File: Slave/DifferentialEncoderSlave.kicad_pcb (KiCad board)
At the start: 4 copper layers, 52.5 x 35.2 mm, 15 parts, among them J1 Conn_01x04, U1 LTC2850xS8, U2 MA730, U3 AZ1117-3.3

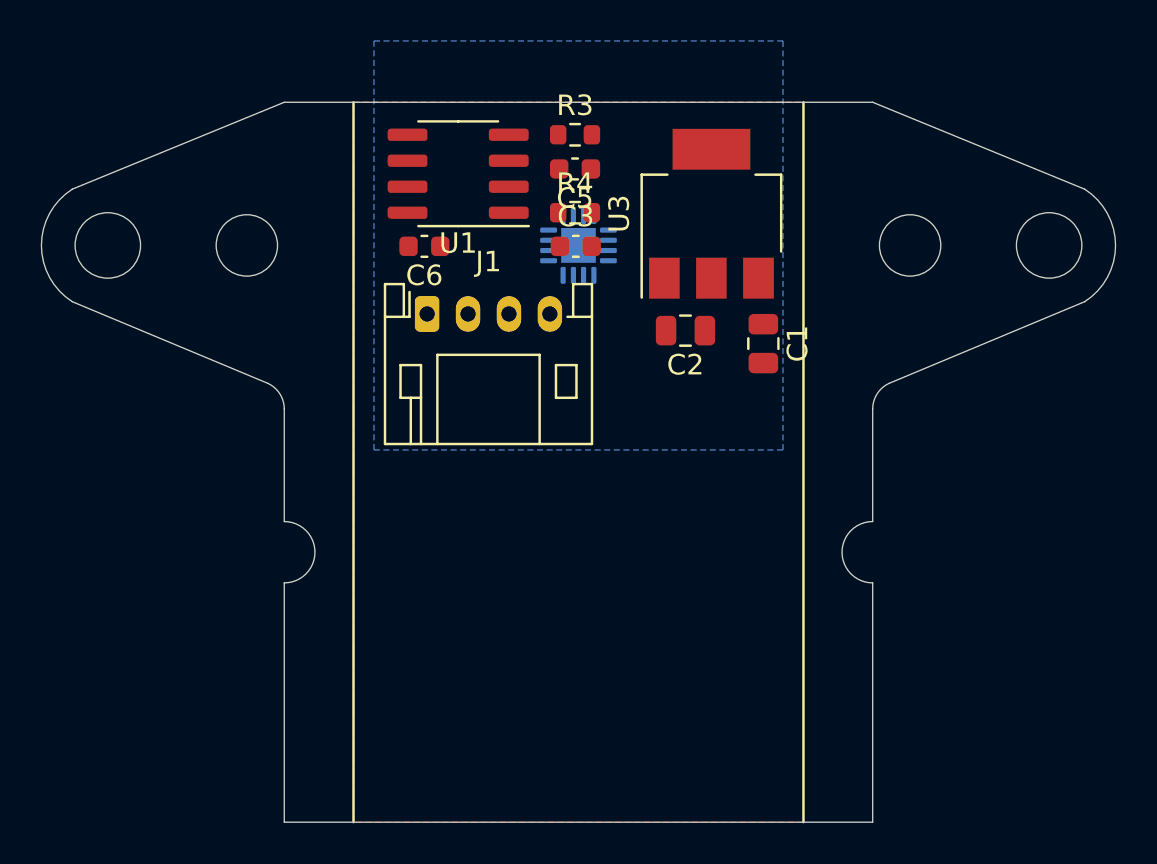
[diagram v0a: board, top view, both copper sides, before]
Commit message: Finish laying out encoder board
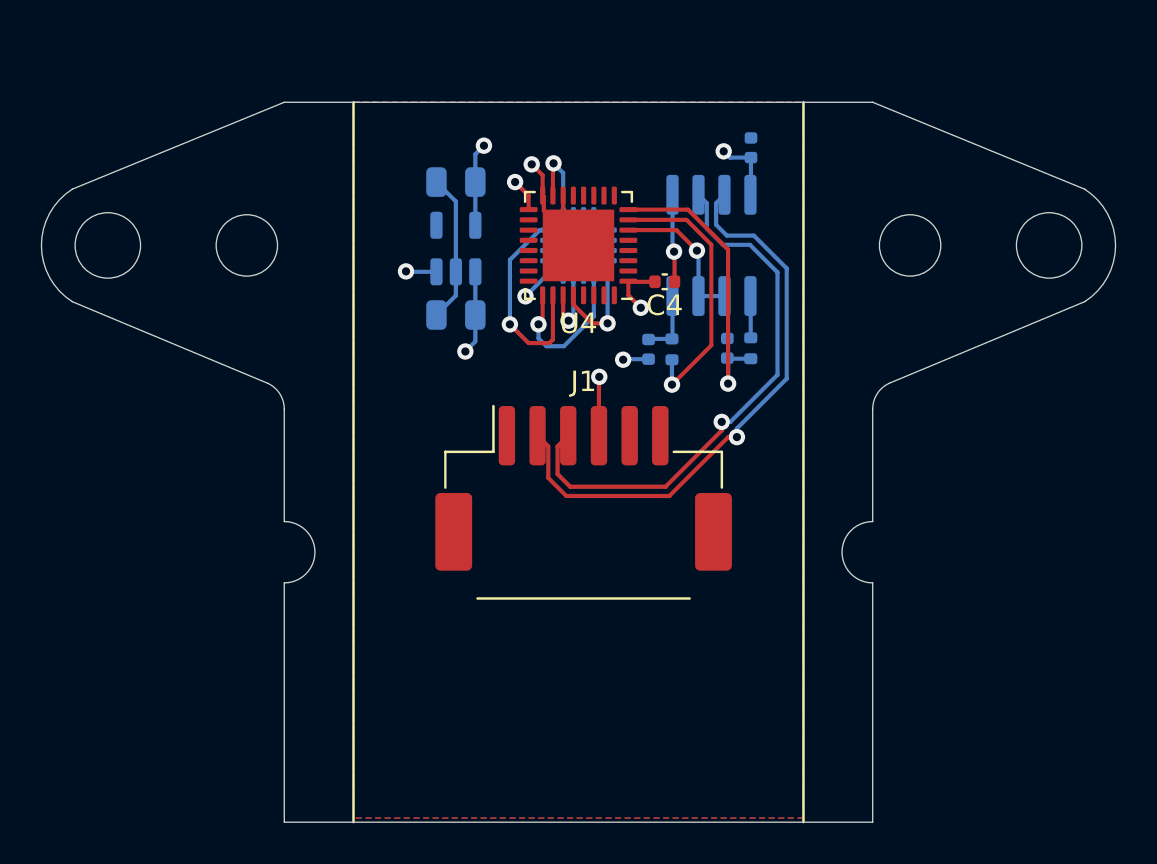
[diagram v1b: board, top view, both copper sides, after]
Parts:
- removed the U3 at (128.5, 66.5)
- added C4: 100nF, Capacitor_SMD:C_0402_1005Metric, F.Cu at (126.2, 69.8)
- added U2: LP5907MFX-3.3, Package_TO_SOT_SMD:SOT-23-5, B.Cu at (116.0, 68.2)
- added U4: STM32G4A1KEU4, Package_DFN_QFN:UFQFPN-32-1EP_5x5mm_P0.5mm_EP3.5x3.5mm, F.Cu at (122.0, 68.0)
- C1: renamed from C6; footprint Capacitor_SMD:C_0603_1608Metric -> Capacitor_SMD:C_0402_1005Metric; moved to B.Cu
- C2: renamed from C3; footprint Capacitor_SMD:C_0603_1608Metric -> Capacitor_SMD:C_0402_1005Metric; moved to B.Cu
- C3: renamed from C5; footprint Capacitor_SMD:C_0603_1608Metric -> Capacitor_SMD:C_0402_1005Metric; moved to B.Cu
- C5: renamed from C1; moved to B.Cu
- C6: renamed from C2; moved to B.Cu
- J1: value Conn_01x04 -> Conn_01x06; footprint Connector_JST:JST_PH_S4B-PH-K_1x04_P2.00mm_Horizontal -> Connector_Molex:Molex_CLIK-Mate_502585-0670_1x06-1MP_P1.50mm_Horizontal
- R1: renamed from R4; footprint Resistor_SMD:R_0603_1608Metric -> Resistor_SMD:R_0402_1005Metric; moved to B.Cu
- R2: renamed from R3; footprint Resistor_SMD:R_0603_1608Metric -> Resistor_SMD:R_0402_1005Metric; moved to B.Cu
- U1: moved to B.Cu
- moved C1 16.7 mm to (130.4, 63.2), turned to -90 degrees
- moved C5 15.1 mm to (116.0, 71.4), turned to 180 degrees
- moved C6 13.4 mm to (116.0, 64.9)
- moved U1 12.9 mm to (128.5, 68.0), turned to 90 degrees
- moved R2 11.5 mm to (126.6, 73.1), turned to -90 degrees
- moved J1 11.5 mm to (122.2, 79.9)
- moved R1 10.9 mm to (130.4, 73.0), turned to -90 degrees
- moved C3 9.52 mm to (125.4, 73.1), turned to 90 degrees
- moved C2 8.93 mm to (129.3, 73.0), turned to -90 degrees
- renumbered U2 to U3
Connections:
- net /RS485_B renamed /RS485_-
- net /UART_RX renamed /USART2_RX
- J1 pad 1: /RS485_A -> +5V
- J1 pad 3: +5V -> /RS485_+
- R2 pad 2: /UART_TX -> /USART2_TX
- U1 pad 2: /~{RE} -> /USART2_DE
- U1 pad 3: /DE -> /USART2_DE
- U1 pad 6: /RS485_A -> /RS485_+
- U3 pad 12: /CLK -> /SPI3_SCK
- U3 pad 4: unconnected-(U2-Pad4) -> /SPI3_MOSI
- U3 pad 5: /CSn -> /SPI3_NSS
- U3 pad 7: /MISO -> /SPI3_MISO
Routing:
- net GNDD: track 0.00 -> 29.0 mm, vias 0 -> 5
- net /RS485_-: track 0.00 -> 28.3 mm, vias 0 -> 1
- net /RS485_+: track 0.00 -> 26.8 mm, vias 0 -> 1
- net /USART2_RX: track 0.00 -> 14.7 mm, vias 0 -> 1
- net /USART2_TX: track 0.00 -> 13.4 mm, vias 0 -> 1
- net +3V3: track 0.00 -> 12.9 mm, vias 0 -> 4
- net /SPI3_SCK: track 0.00 -> 10.4 mm, vias 0 -> 1
- net +5V: track 0.00 -> 8.88 mm, vias 0 -> 3
- net /SPI3_NSS: track 0.00 -> 7.67 mm, vias 0 -> 1
- net /USART2_DE: track 0.00 -> 7.29 mm, vias 0 -> 1
- net /SPI3_MOSI: track 0.00 -> 5.58 mm, vias 0 -> 1
- net /SPI3_MISO: track 0.00 -> 3.67 mm, vias 0 -> 1
- net /DI: track 0.00 -> 3.30 mm
- net /RO: track 0.00 -> 2.05 mm
- added copper zone on In1.Cu, net +3V3
- added copper zone on F.Cu, net +5V
- removed copper zone on F.Cu, net +3V3
- removed copper zone on In1.Cu, net +5V

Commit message: Change pinout on STM32G4, add thermistor header, add test points
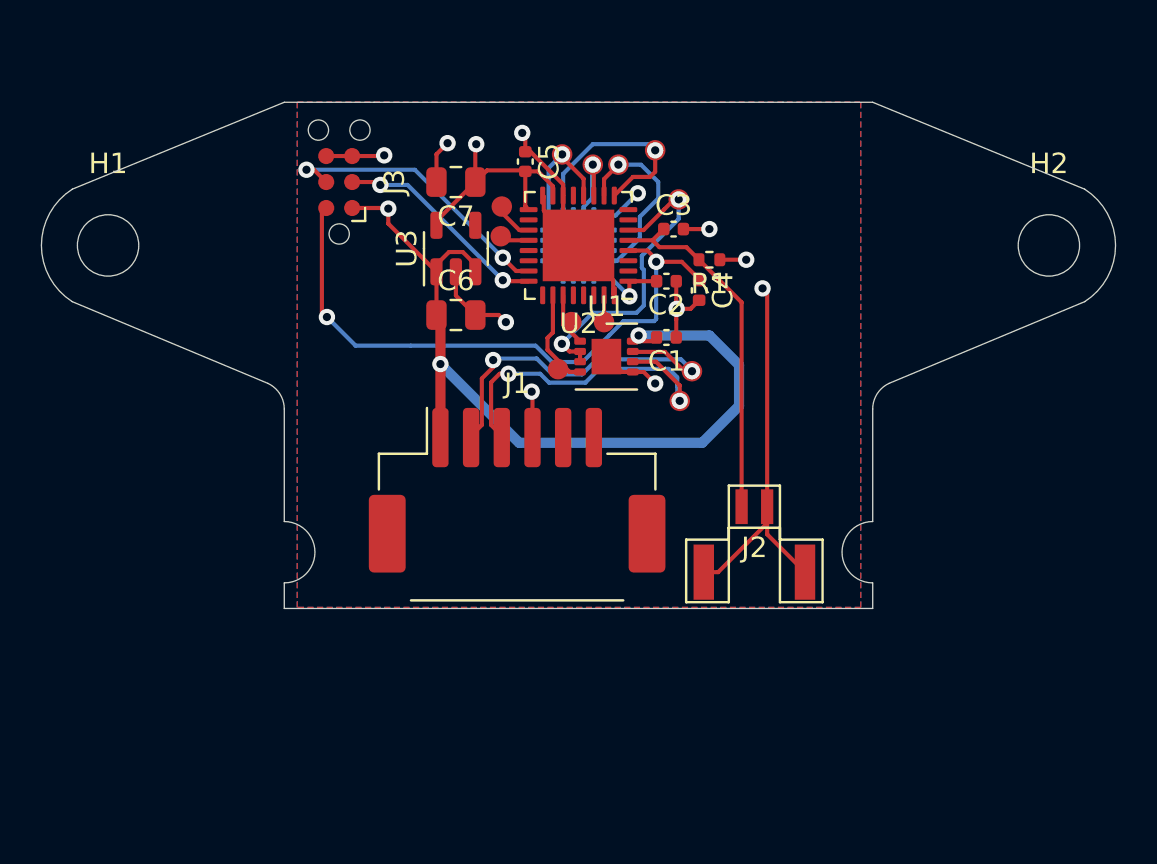
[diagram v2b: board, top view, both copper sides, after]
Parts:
- removed the C2 at (129.3, 73.0)
- removed H3: MountingHole, MountingHole:MountingHole_3mm
- removed H5, H6: MountingHole, MountingHole:MountingHole_3.2mm_M3_DIN965
- removed R2: 680, Resistor_SMD:R_0402_1005Metric
- added C4: 100nF, Capacitor_SMD:C_0402_1005Metric, F.Cu at (127.9, 70.2)
- added C5: 100nF, Capacitor_SMD:C_0402_1005Metric, F.Cu at (119.4, 63.9)
- added H2: MountingHole, MountingHole:MountingHole_3mm, F.Cu at (145.0, 68.0)
- added J2: Thermistor, ODrive_KiCad:JST_GH_SM02B, F.Cu at (130.6, 80.8)
- added J3: Conn_01x06, Connector:Tag-Connect_TC2030-IDC-NL_2x03_P1.27mm_Vertical, F.Cu at (110.3, 64.9)
- added TP1: TestPoint, ODrive_KiCad:TestPoint_Pad_D1.0mm, F.Cu at (123.2, 71.8)
- added TP10: TestPoint, ODrive_KiCad:TestPoint_Pad_D1.0mm, F.Cu at (121.2, 63.5)
- added TP11: TestPoint, ODrive_KiCad:TestPoint_Pad_D1.0mm, F.Cu at (127.5, 74.2)
- added TP12: TestPoint, ODrive_KiCad:TestPoint_Pad_D1.0mm, F.Cu at (127.0, 75.6)
- added TP2: TestPoint, ODrive_KiCad:TestPoint_Pad_D1.0mm, F.Cu at (118.2, 66.1)
- added TP3: TestPoint, ODrive_KiCad:TestPoint_Pad_D1.0mm, F.Cu at (118.2, 67.5)
- added TP4: TestPoint, ODrive_KiCad:TestPoint_Pad_D1.0mm, F.Cu at (126.9, 65.8)
- added TP5: TestPoint, ODrive_KiCad:TestPoint_Pad_D1.0mm, F.Cu at (121.0, 74.0)
- added TP6: TestPoint, ODrive_KiCad:TestPoint_Pad_D1.0mm, F.Cu at (121.7, 71.8)
- added TP7: TestPoint, ODrive_KiCad:TestPoint_Pad_D1.0mm, F.Cu at (125.8, 63.4)
- added TP8: TestPoint, ODrive_KiCad:TestPoint_Pad_D1.0mm, F.Cu at (124.0, 64.0)
- added TP9: TestPoint, ODrive_KiCad:TestPoint_Pad_D1.0mm, F.Cu at (122.7, 64.0)
- C1: moved to F.Cu
- C3: value 22pF -> 2.2uF; moved to F.Cu
- C6: renamed from C5; moved to F.Cu
- C7: renamed from C6; moved to F.Cu
- J1: value Conn_01x06 -> Main
- R1: value 680 -> 4.7k; moved to F.Cu
- U1: value LTC2850xS8 -> ADM4852; footprint Package_SO:SOIC-8_3.9x4.9mm_P1.27mm -> Package_CSP:LFCSP-8-1EP_3x3mm_P0.5mm_EP1.45x1.74mm; moved to F.Cu
- U3: renamed from U2; moved to F.Cu
- moved H1 39.2 mm to (99.0, 68.0)
- moved C1 10.2 mm to (126.3, 72.5), turned to 180 degrees
- moved U1 7.48 mm to (123.4, 73.4), turned to 0 degrees
- moved C3 6.01 mm to (126.7, 67.2), turned to 0 degrees
- moved R1 4.78 mm to (128.4, 68.7), turned to 180 degrees
- moved J1 3.25 mm to (119.0, 80.0)
- moved C2 0.09 mm to (126.3, 69.8)
- turned C6 to 0 degrees
- turned U4 to 0 degrees
- renumbered C4 to C2, U4 to U2, U3 to U4
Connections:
- net /RS485_+ renamed /RS485_P
- net /RS485_- renamed /RS485_N
- net /USB_DM renamed /USB_DN
- C3 pad 1: GNDD -> /TEMP
- C3 pad 2: /DI -> GNDD
- R1 pad 1: /RO -> +3V3
- R1 pad 2: /USART2_RX -> /TEMP
- U1 pad 1: /RO -> /USART2_RX
- U1 pad 4: /DI -> /USART2_TX
- U2 pad 10: unconnected-(U4-Pad10) -> /SPI1_SCK
- U2 pad 11: unconnected-(U4-Pad11) (its old number) -> /SPI1_MISO
- U2 pad 12: /ADC2_IN4 -> /SPI1_MOSI
- U2 pad 13: /ADC1_IN15 -> unconnected-(U2-Pad13)
- U2 pad 19: unconnected-(U4-Pad19) -> /USART1_TX
- U2 pad 20: unconnected-(U4-Pad20) -> /USART1_RX
- U2 pad 23: unconnected-(U4-Pad23) -> /SWDIO
- U2 pad 24: unconnected-(U4-Pad24) -> /SWCLK
- U2 pad 25: /SPI3_NSS -> unconnected-(U2-Pad25)
- U2 pad 26: /SPI3_SCK -> /USART2_TX
- U2 pad 27: /SPI3_MISO -> /USART2_RX
- U2 pad 28: /SPI3_MOSI -> /I2S3_SD
- U2 pad 31: (no net) -> /BOOT0
- U2 pad 32: (no net) -> GNDD
- U2 pad 4: (no net) -> /~{RESET}
- U2 pad 5: /ADC1_IN1 -> /TEMP
- U2 pad 7: /USART2_TX -> unconnected-(U2-Pad7)
- U2 pad 8: /USART2_RX -> unconnected-(U2-Pad8)
- U2 pad 9: unconnected-(U4-Pad9) (its old number) -> /SPI1_NSS
- U4 pad 12: /SPI3_SCK -> /SPI1_SCK
- U4 pad 4: /SPI3_MOSI -> /SPI1_MOSI
- U4 pad 5: /SPI3_NSS -> /SPI1_NSS
- U4 pad 7: /SPI3_MISO -> /SPI1_MISO
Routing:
- net +5V: track 8.88 -> 43.2 mm
- net GNDD: track 29.0 -> 59.9 mm, vias 5 -> 10
- net /~{RESET}: track 0.00 -> 30.3 mm, vias 0 -> 2
- net /TEMP: track 0.00 -> 17.6 mm
- net /SWDIO: track 0.00 -> 14.1 mm, vias 0 -> 2
- net /USART2_RX: track 14.7 -> 2.59 mm, vias 1 -> 0
- net /SPI1_NSS: track 0.00 -> 10.8 mm, vias 0 -> 1
- net /SWCLK: track 0.00 -> 10.6 mm, vias 0 -> 2
- net /SPI3_SCK: track 10.4 -> 0.00 mm, vias 1 -> 0
- net /RS485_N: track 28.3 -> 18.1 mm, vias 1 -> 2
- net /RS485_P: track 26.8 -> 17.5 mm, vias 1 -> 2
- net /SPI1_SCK: track 0.00 -> 9.21 mm, vias 0 -> 1
- net /USART2_TX: track 13.4 -> 4.82 mm, vias 1 -> 0
- net /USART2_DE: track 7.29 -> 15.4 mm, vias 1 -> 2
- net /SPI3_NSS: track 7.67 -> 0.00 mm, vias 1 -> 0
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- added copper zone on B.Cu, net +5V
- added copper zone on F.Cu, net GNDD
- removed copper zone on F.Cu, net +5V
- removed copper zone on B.Cu, net GNDD
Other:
- board size 52.5 x 35.2 mm -> 52.5 x 24.8 mm

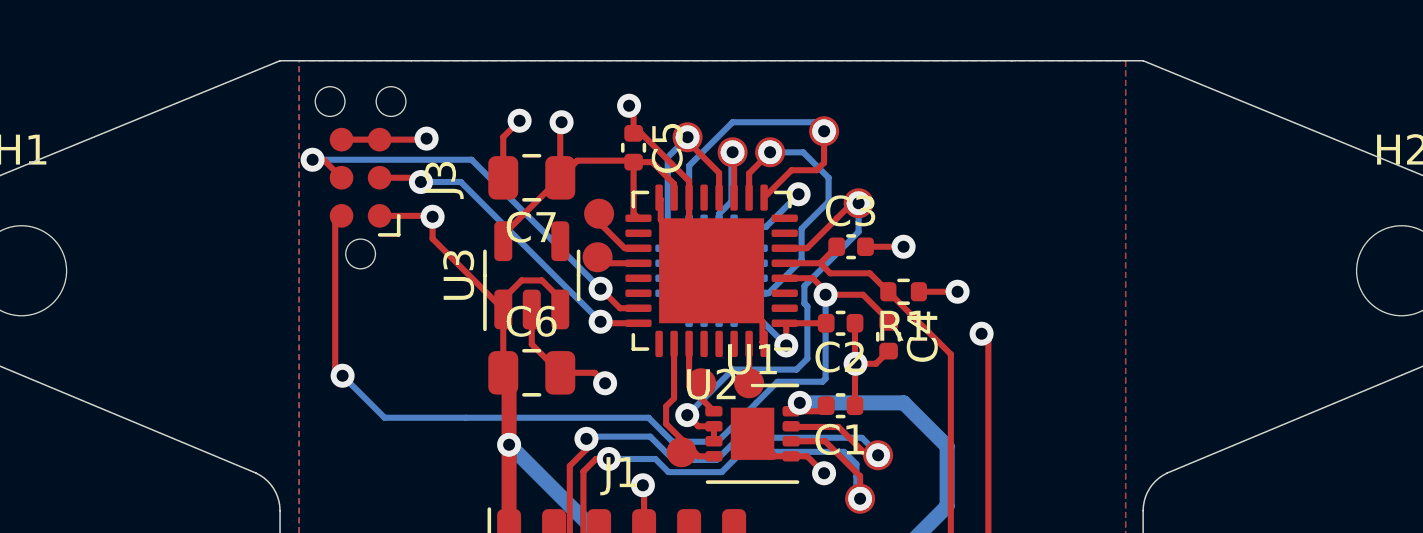
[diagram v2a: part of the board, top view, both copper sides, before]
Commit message: Add narrow mounting holes
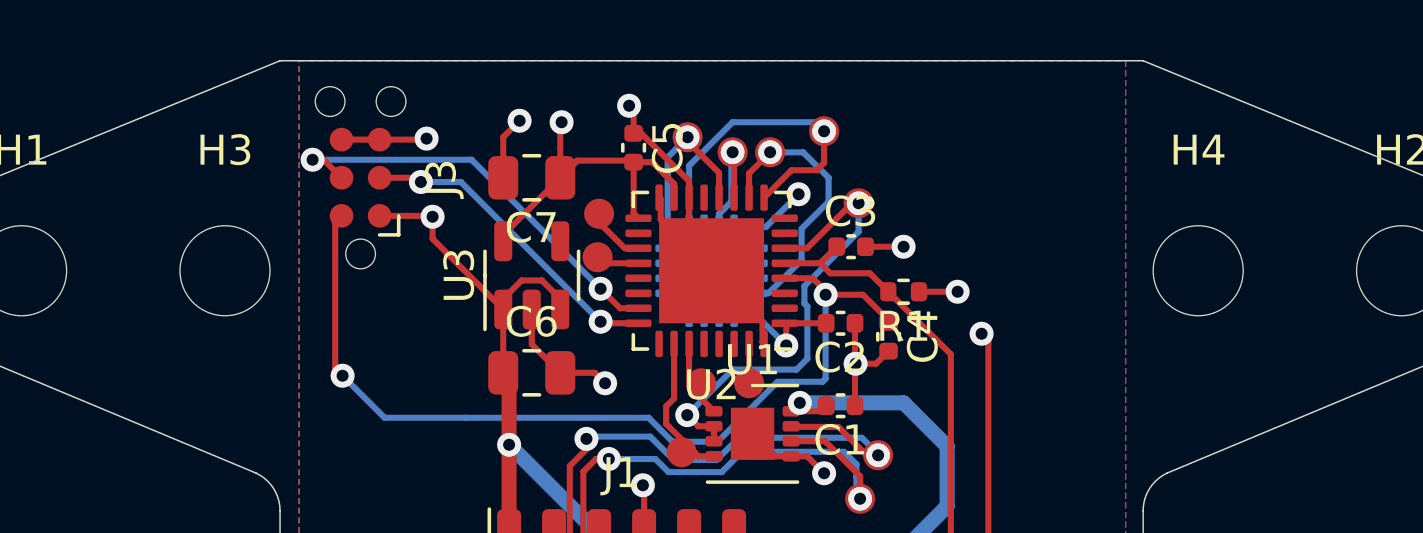
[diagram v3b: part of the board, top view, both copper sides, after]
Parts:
- added H3: MountingHole, MountingHole:MountingHole_3mm, F.Cu at (105.8, 68.0)
- added H4: MountingHole, MountingHole:MountingHole_3mm, F.Cu at (138.2, 68.0)
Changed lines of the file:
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@@
+  )
+  (footprint "MountingHole:MountingHole_3mm" (layer "F.Cu")
+    (at 105.78 68)
+    (descr "Mounting Hole 3mm, no annular")
+    (tags "mounting hole 3mm no annular")
+    (property "Sheetfile" "DifferentialEncoderSlave.kicad_sch")
+    (property "Sheetname" "")
+    (attr exclude_from_pos_files)
+    (fp_text reference "H3" (at 0 -4) (layer "F.SilkS")
+      (effects (font (size 1 1) (thickness 0.15)))
+    )
+    (fp_text value "MountingHole" (at 0 4) (layer "F.Fab")
+      (effects (font (size 1 1) (thickness 0.15)))
+    )
+    (fp_text user "${REFERENCE}" (at 0 0) (layer "F.Fab")
+      (effects (font (size 1 1) (thickness 0.15)))
+    )
+    (fp_circle (center 0 0) (end 3 0) (layer "Cmts.User") (width 0.15) (fill none))
+    (fp_circle (center 0 0) (end 3.25 0) (layer "F.CrtYd") (width 0.05) (fill none))
+    (pad "" np_thru_hole circle (at 0 0) (size 3 3) (drill 3) (layers *.Cu *.Mask))
   )
   (footprint "MountingHole:MountingHole_3mm" (layer "F.Cu")
@@
     )
   )
+  (footprint "MountingHole:MountingHole_3mm" (layer "F.Cu")
+    (at 138.22 68)
+    (descr "Mounting Hole 3mm, no annular")
+    (tags "mounting hole 3mm no annular")
+    (property "Sheetfile" "DifferentialEncoderSlave.kicad_sch")
+    (property "Sheetname" "")
+    (attr exclude_from_pos_files)
+    (fp_text reference "H4" (at 0 -4) (layer "F.SilkS")
+      (effects (font (size 1 1) (thickness 0.15)))
+    )
+    (fp_text value "MountingHole" (at 0 4) (layer "F.Fab")
+      (effects (font (size 1 1) (thickness 0.15)))
+    )
+    (fp_text user "${REFERENCE}" (at 0 0) (layer "F.Fab")
+      (effects (font (size 1 1) (thickness 0.15)))
+    )
+    (fp_circle (center 0 0) (end 3 0) (layer "Cmts.User") (width 0.15) (fill none))
+    (fp_circle (center 0 0) (end 3.25 0) (layer "F.CrtYd") (width 0.05) (fill none))
+    (pad "" np_thru_hole circle (at 0 0) (size 3 3) (drill 3) (layers *.Cu *.Mask))
+  )
   (footprint "Package_DFN_QFN:QFN-16-1EP_3x3mm_P0.5mm_EP1.7x1.7mm" (layer "B.Cu")
